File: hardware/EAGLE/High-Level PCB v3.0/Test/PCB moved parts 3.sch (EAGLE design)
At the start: 58 parts, among them IC1 MCP2551, IC2 DS8921, IC3 DS8921, J1 Optical Mouse, J2 RaspπUart, J8 DB9 Plug, J9 CAN Output, U1 COMPASS, U2 LLSHIFTER, U3 GPS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

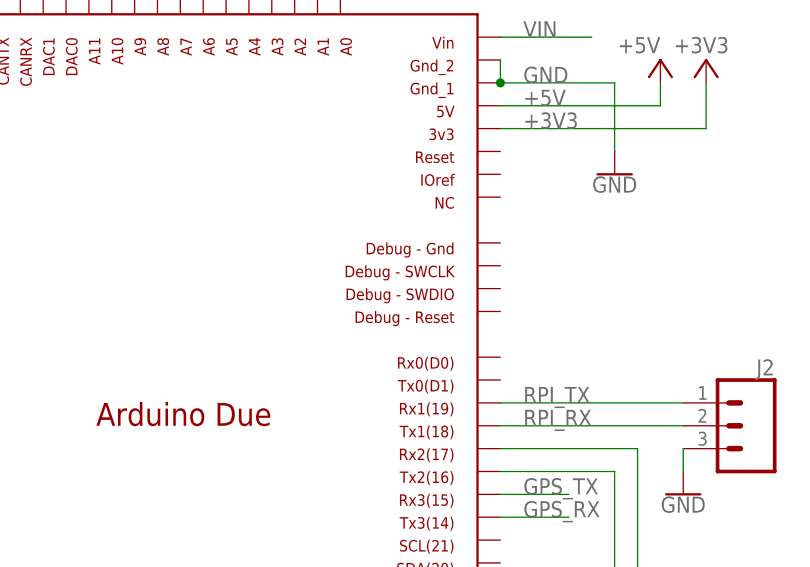
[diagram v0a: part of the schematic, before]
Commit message: The 3 board has no air wires!
And it has thick power traces.
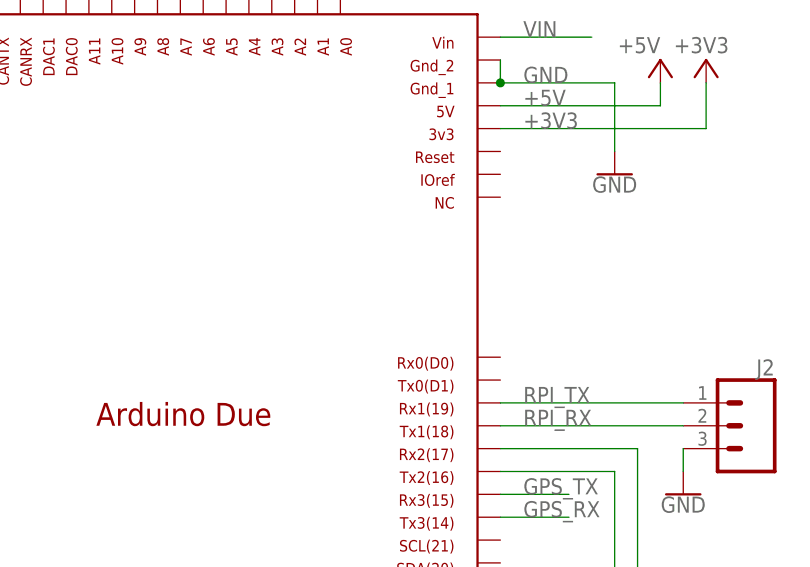
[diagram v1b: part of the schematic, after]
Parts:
- J2: device tx_rxRasp:CONN_02 -> ELCano_Footprints:TXRX_2RSPPI
- U1: device ELCOMPASS:ELCOMPASS -> ELCano_Footprints:ELCOMPASS
- U2: device ELSHIFTER:ELSHIFTER -> ELCano_Footprints:ELSHIFTER
- U3: device ELGPS:ELGPS -> ELCano_Footprints:ELGPS
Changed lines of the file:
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@@
 <class number="0" name="default" width="0" drill="0">
 </class>
-<class number="1" name="Power" width="0.508" drill="0.3048">
+<class number="1" name="Power" width="0.254" drill="0.3048">
 <clearance class="1" value="0.254"/>
 </class>
@@
 <part name="TP1" library="testpad" library_urn="urn:adsk.eagle:library:385" deviceset="TP" device="PAD1-17" package3d_urn="urn:adsk.eagle:package:27949/1"/>
 <part name="TP2" library="testpad" library_urn="urn:adsk.eagle:library:385" deviceset="TP" device="PAD1-17" package3d_urn="urn:adsk.eagle:package:27949/1"/>
-<part name="U2" library="ELSHIFTER" deviceset="ELSHIFTER" device="" value="LLSHIFTER"/>
-<part name="U1" library="ELCOMPASS" deviceset="ELCOMPASS" device="" value="COMPASS"/>
-<part name="U3" library="ELGPS" deviceset="ELGPS" device="" value="GPS"/>
-<part name="J2" library="tx_rxRasp" deviceset="CONN_02" device="" value="RaspπUart"/>
+<part name="U2" library="ELCano_Footprints" deviceset="ELSHIFTER" device="" value="LLSHIFTER"/>
+<part name="U1" library="ELCano_Footprints" deviceset="ELCOMPASS" device="" value="COMPASS"/>
+<part name="U3" library="ELCano_Footprints" deviceset="ELGPS" device="" value="GPS"/>
+<part name="J2" library="ELCano_Footprints" deviceset="TXRX_2RSPPI" device="" value="RaspπUart"/>
 <part name="GND14" library="SparkFun-PowerSymbols" deviceset="GND" device=""/>
 <part name="U$1" library="ELCano_Footprints" deviceset="ELGYRO_L3GD20H" device="" value="Gyro"/>
